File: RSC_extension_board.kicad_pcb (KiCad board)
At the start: 2 copper layers, 65 x 56.5 mm, 111 parts, among them J1 NPTC202KFMS-RC, J10 Conn_01x04, J11 Conn_01x03, J12 Conn_01x03, J13 Conn_01x10, J16 USB_C_Receptacle_PowerOnly_6P, J2 Conn_01x02, J4 TSM-120-02-F-DH, J5 Conn_01x02, J6 Conn_01x03, J7 Conn_01x03, J8 Conn_01x03, J9 PRT-14417, Q1 2N7002-7-F, Q2 BSS138, Q3 DMP3013SFV, Q4 DMP3013SFV, U3 LMR604403SRAKR, U4 LMR604403SRAKR, U5 CYPD3177-24LQ

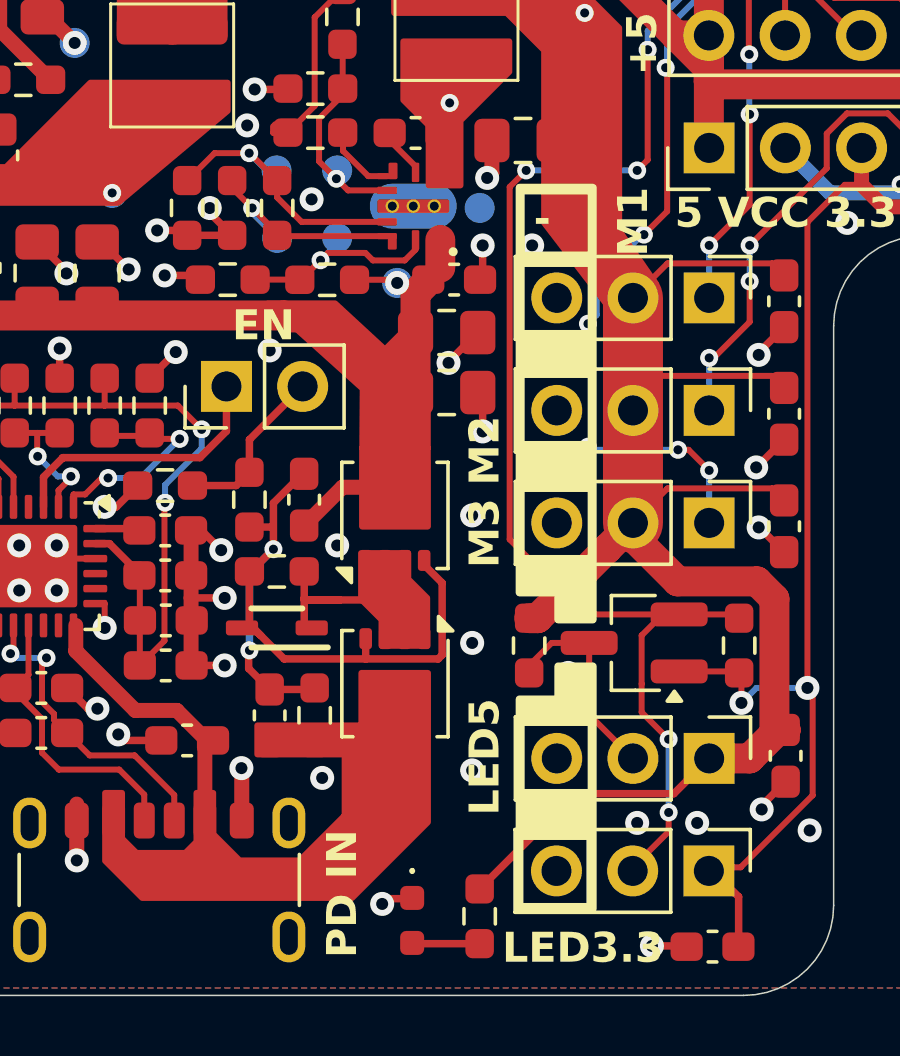
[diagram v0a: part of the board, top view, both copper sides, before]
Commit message: WIP - need to validate revA neopx working at curr pin
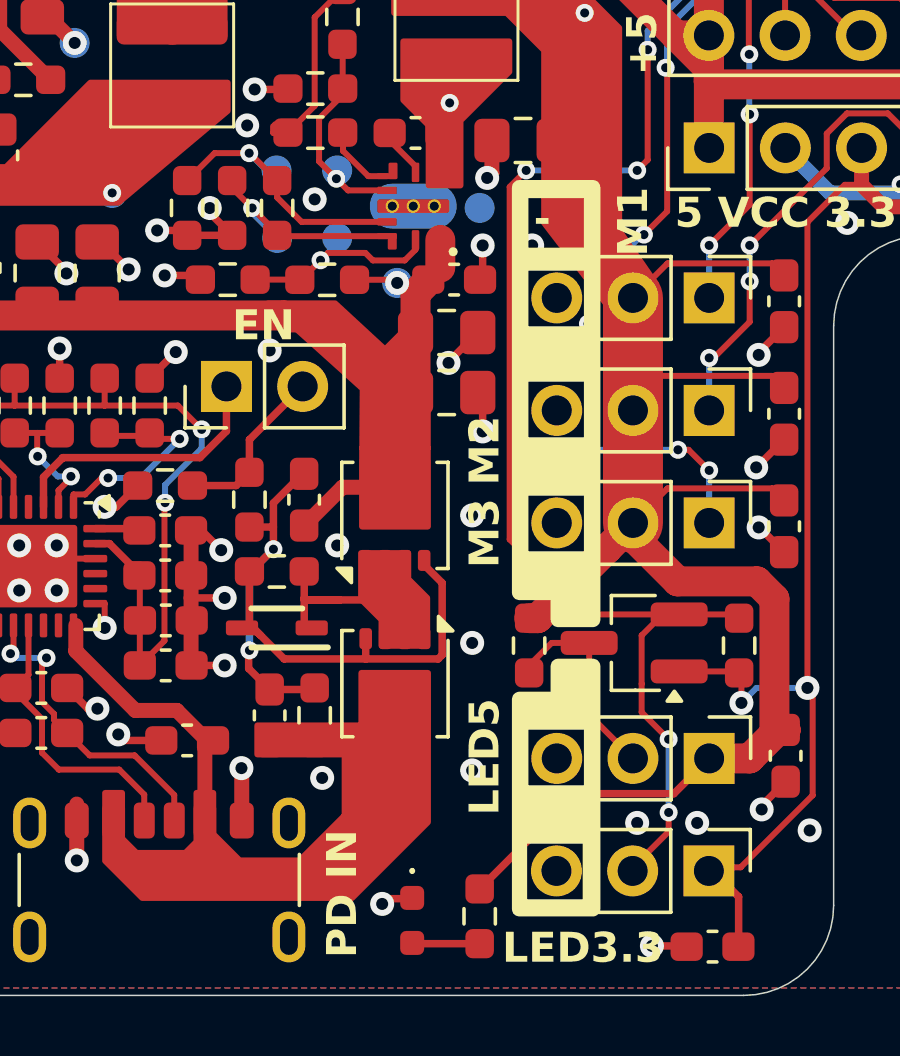
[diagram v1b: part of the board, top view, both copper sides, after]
